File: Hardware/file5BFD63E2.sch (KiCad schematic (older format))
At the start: 14 parts, among them J18 Power_Connector_IO, J20 Digital_Connector_IO, J21 CV_Connector_IO, J22 Pot_Connector_IO, J23 Attenuverter_Connector_IO, J28 SID_Audio_Connector_IO

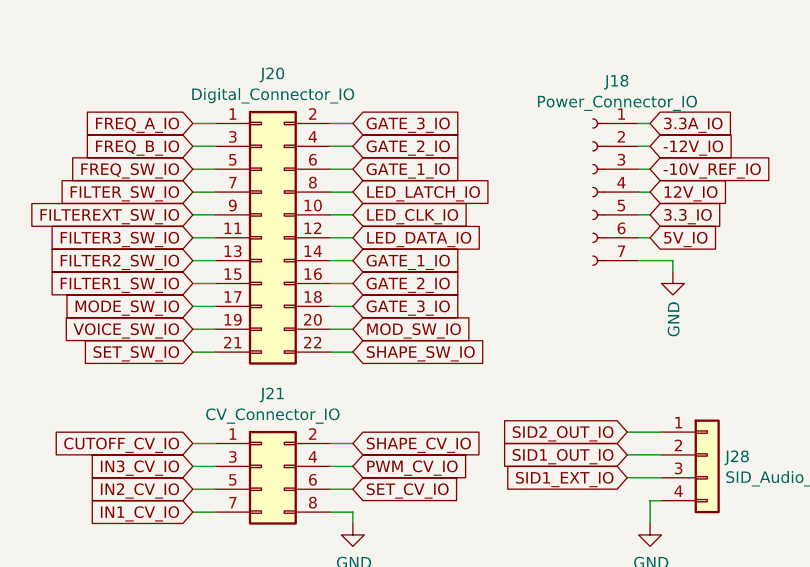
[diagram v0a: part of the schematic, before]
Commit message: Added some connector routing
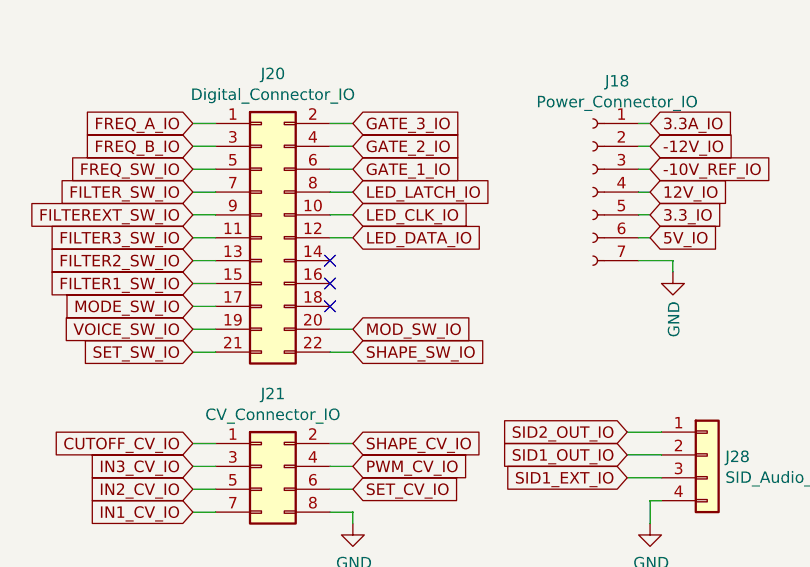
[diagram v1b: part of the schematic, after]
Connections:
- net GATE_1_IO: no longer J20.14 (Pin_14)
- net GATE_2_IO: no longer J20.16 (Pin_16)
- net GATE_3_IO: no longer J20.18 (Pin_18)
- no-connect marks 0 -> 3
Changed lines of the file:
@@
 Text GLabel 1750 3400 0    50   Input ~ 0
 FREQ_B_IO
-Text GLabel 2450 4100 2    50   Input ~ 0
-GATE_3_IO
-Text GLabel 2450 4000 2    50   Input ~ 0
-GATE_2_IO
-Text GLabel 2450 3900 2    50   Input ~ 0
-GATE_1_IO
 Text GLabel 2450 3800 2    50   Input ~ 0
 LED_DATA_IO
@@
 Wire Wire Line
 	2350 4200 2450 4200
-Wire Wire Line
-	2350 4100 2450 4100
-Wire Wire Line
-	2350 4000 2450 4000
-Wire Wire Line
-	2350 3900 2450 3900
 Wire Wire Line
 	2350 3800 2450 3800
@@
 	1    0    0    -1
 $EndComp
+NoConn ~ 2350 3900
+NoConn ~ 2350 4000
+NoConn ~ 2350 4100
 $EndSCHEMATC

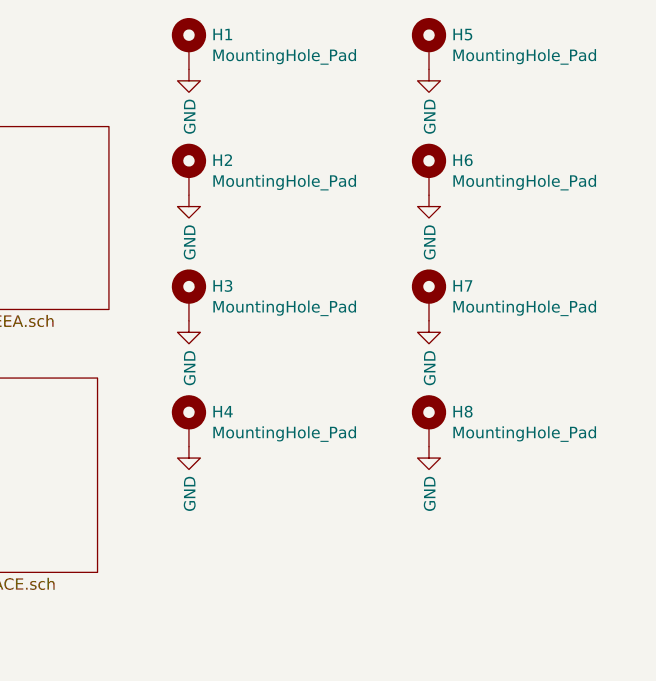
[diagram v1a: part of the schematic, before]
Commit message: Corrected layout and schematic to single standoff
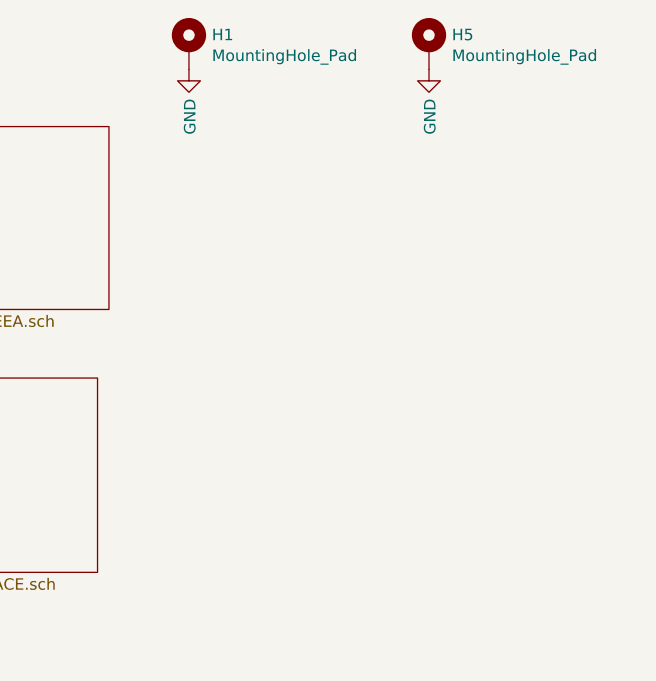
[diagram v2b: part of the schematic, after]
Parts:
- removed H2, H3, H4, H6, H7, H8: MountingHole_Pad, MountingHole:MountingHole_3.2mm_M3_DIN965_Pad, symbol Mechanical:MountingHole_Pad
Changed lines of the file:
@@
-$EndComp
-$Comp
-L Mechanical:MountingHole_Pad H6
-U 1 1 5BE3763A
-P 7100 2900
-F 0 "H6" H 7200 2951 50  0000 L CNN
-F 1 "MountingHole_Pad" H 7200 2860 50  0000 L CNN
-F 2 "MountingHole:MountingHole_3.2mm_M3_DIN965_Pad" H 7100 2900 50  0001 C CNN
-F 3 "~" H 7100 2900 50  0001 C CNN
-	1    7100 2900
-	1    0    0    -1
-$EndComp
-$Comp
-L Mechanical:MountingHole_Pad H7
-U 1 1 5BE3766D
-P 7100 3450
-F 0 "H7" H 7200 3501 50  0000 L CNN
-F 1 "MountingHole_Pad" H 7200 3410 50  0000 L CNN
-F 2 "MountingHole:MountingHole_3.2mm_M3_DIN965_Pad" H 7100 3450 50  0001 C CNN
-F 3 "~" H 7100 3450 50  0001 C CNN
-	1    7100 3450
-	1    0    0    -1
-$EndComp
-$Comp
-L Mechanical:MountingHole_Pad H8
-U 1 1 5BE376A0
-P 7100 4000
-F 0 "H8" H 7200 4051 50  0000 L CNN
-F 1 "MountingHole_Pad" H 7200 3960 50  0000 L CNN
-F 2 "MountingHole:MountingHole_3.2mm_M3_DIN965_Pad" H 7100 4000 50  0001 C CNN
-F 3 "~" H 7100 4000 50  0001 C CNN
-	1    7100 4000
-	1    0    0    -1
 $EndComp
 $Comp
@@
 	1    0    0    -1
 $EndComp
-$Comp
-L Mechanical:MountingHole_Pad H2
-U 1 1 5BE3F338
-P 6050 2900
-F 0 "H2" H 6150 2951 50  0000 L CNN
-F 1 "MountingHole_Pad" H 6150 2860 50  0000 L CNN
-F 2 "MountingHole:MountingHole_3.2mm_M3_DIN965_Pad" H 6050 2900 50  0001 C CNN
-F 3 "~" H 6050 2900 50  0001 C CNN
-	1    6050 2900
-	1    0    0    -1
-$EndComp
-$Comp
-L Mechanical:MountingHole_Pad H3
-U 1 1 5BE3F33F
-P 6050 3450
-F 0 "H3" H 6150 3501 50  0000 L CNN
-F 1 "MountingHole_Pad" H 6150 3410 50  0000 L CNN
-F 2 "MountingHole:MountingHole_3.2mm_M3_DIN965_Pad" H 6050 3450 50  0001 C CNN
-F 3 "~" H 6050 3450 50  0001 C CNN
-	1    6050 3450
-	1    0    0    -1
-$EndComp
-$Comp
-L Mechanical:MountingHole_Pad H4
-U 1 1 5BE3F346
-P 6050 4000
-F 0 "H4" H 6150 4051 50  0000 L CNN
-F 1 "MountingHole_Pad" H 6150 3960 50  0000 L CNN
-F 2 "MountingHole:MountingHole_3.2mm_M3_DIN965_Pad" H 6050 4000 50  0001 C CNN
-F 3 "~" H 6050 4000 50  0001 C CNN
-	1    6050 4000
-	1    0    0    -1
-$EndComp
-$Comp
-L power:GND #PWR?
-U 1 1 5BE41CB1
-P 6050 4100
-AR Path="/5C5B0291/5BE41CB1" Ref="#PWR?"  Part="1"
-AR Path="/5BFD63E3/5BE41CB1" Ref="#PWR0163"  Part="1"
-F 0 "#PWR0163" H 6050 3850 50  0001 C CNN
-F 1 "GND" V 6055 3972 50  0000 R CNN
-F 2 "" H 6050 4100 50  0001 C CNN
-F 3 "" H 6050 4100 50  0001 C CNN
-	1    6050 4100
-	1    0    0    -1
-$EndComp
-$Comp
-L power:GND #PWR?
-U 1 1 5BE41D02
-P 7100 4100
-AR Path="/5C5B0291/5BE41D02" Ref="#PWR?"  Part="1"
-AR Path="/5BFD63E3/5BE41D02" Ref="#PWR0164"  Part="1"
-F 0 "#PWR0164" H 7100 3850 50  0001 C CNN
-F 1 "GND" V 7105 3972 50  0000 R CNN
-F 2 "" H 7100 4100 50  0001 C CNN
-F 3 "" H 7100 4100 50  0001 C CNN
-	1    7100 4100
-	1    0    0    -1
-$EndComp
-$Comp
-L power:GND #PWR?
-U 1 1 5BE435B9
-P 6050 3000
-AR Path="/5C5B0291/5BE435B9" Ref="#PWR?"  Part="1"
-AR Path="/5BFD63E3/5BE435B9" Ref="#PWR0165"  Part="1"
-F 0 "#PWR0165" H 6050 2750 50  0001 C CNN
-F 1 "GND" V 6055 2872 50  0000 R CNN
-F 2 "" H 6050 3000 50  0001 C CNN
-F 3 "" H 6050 3000 50  0001 C CNN
-	1    6050 3000
-	1    0    0    -1
-$EndComp
-$Comp
-L power:GND #PWR?
-U 1 1 5BE435E0
-P 7100 3000
-AR Path="/5C5B0291/5BE435E0" Ref="#PWR?"  Part="1"
-AR Path="/5BFD63E3/5BE435E0" Ref="#PWR0166"  Part="1"
-F 0 "#PWR0166" H 7100 2750 50  0001 C CNN
-F 1 "GND" V 7105 2872 50  0000 R CNN
-F 2 "" H 7100 3000 50  0001 C CNN
-F 3 "" H 7100 3000 50  0001 C CNN
-	1    7100 3000
-	1    0    0    -1
-$EndComp
-$Comp
-L power:GND #PWR?
-U 1 1 5BE49823
-P 6050 3550
-AR Path="/5C5B0291/5BE49823" Ref="#PWR?"  Part="1"
-AR Path="/5BFD63E3/5BE49823" Ref="#PWR0167"  Part="1"
-F 0 "#PWR0167" H 6050 3300 50  0001 C CNN
-F 1 "GND" V 6055 3422 50  0000 R CNN
-F 2 "" H 6050 3550 50  0001 C CNN
-F 3 "" H 6050 3550 50  0001 C CNN
-	1    6050 3550
-	1    0    0    -1
-$EndComp
-$Comp
-L power:GND #PWR?
-U 1 1 5BE4984A
-P 7100 3550
-AR Path="/5C5B0291/5BE4984A" Ref="#PWR?"  Part="1"
-AR Path="/5BFD63E3/5BE4984A" Ref="#PWR0168"  Part="1"
-F 0 "#PWR0168" H 7100 3300 50  0001 C CNN
-F 1 "GND" V 7105 3422 50  0000 R CNN
-F 2 "" H 7100 3550 50  0001 C CNN
-F 3 "" H 7100 3550 50  0001 C CNN
-	1    7100 3550
-	1    0    0    -1
-$EndComp

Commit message: Swapped for real oscillator, fixed footprint discrepencies
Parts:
- J18: footprint Connector_PinSocket_2.54mm:PinSocket_1x07_P2.54mm_Vertical_SMD_Pin1Left -> Connector_PinSocket_2.54mm:PinSocket_1x07_P2.54mm_Vertical
- J21, J22: footprint Connector_PinSocket_2.54mm:PinSocket_2x04_P2.54mm_Vertical_SMD -> Connector_PinSocket_2.54mm:PinSocket_2x04_P2.54mm_Vertical
- J23, J28: footprint Connector_PinSocket_2.54mm:PinSocket_1x04_P2.54mm_Vertical_SMD_Pin1Left -> Connector_PinSocket_2.54mm:PinSocket_1x04_P2.54mm_Vertical
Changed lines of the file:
@@
 F 0 "J18" H 3394 4085 50  0000 C CNN
 F 1 "Power_Connector_IO" H 3394 3994 50  0000 C CNN
-F 2 "Connector_PinSocket_2.54mm:PinSocket_1x07_P2.54mm_Vertical_SMD_Pin1Left" H 3500 3600 50  0001 C CNN
+F 2 "Connector_PinSocket_2.54mm:PinSocket_1x07_P2.54mm_Vertical" H 3500 3600 50  0001 C CNN
 F 3 "~" H 3500 3600 50  0001 C CNN
 	1    3500 3600
@@
 F 0 "J21" H 2100 5117 50  0000 C CNN
 F 1 "CV_Connector_IO" H 2100 5026 50  0000 C CNN
-F 2 "Connector_PinSocket_2.54mm:PinSocket_2x04_P2.54mm_Vertical_SMD" H 2050 4800 50  0001 C CNN
+F 2 "Connector_PinSocket_2.54mm:PinSocket_2x04_P2.54mm_Vertical" H 2050 4800 50  0001 C CNN
 F 3 "~" H 2050 4800 50  0001 C CNN
 	1    2050 4800
@@
 F 0 "J22" H 2100 5967 50  0000 C CNN
 F 1 "Pot_Connector_IO" H 2100 5876 50  0000 C CNN
-F 2 "Connector_PinSocket_2.54mm:PinSocket_2x04_P2.54mm_Vertical_SMD" H 2050 5650 50  0001 C CNN
+F 2 "Connector_PinSocket_2.54mm:PinSocket_2x04_P2.54mm_Vertical" H 2050 5650 50  0001 C CNN
 F 3 "~" H 2050 5650 50  0001 C CNN
 	1    2050 5650
@@
 F 0 "J23" H 2129 6192 50  0000 L CNN
 F 1 "Attenuverter_Connector_IO" H 2129 6101 50  0000 L CNN
-F 2 "Connector_PinSocket_2.54mm:PinSocket_1x04_P2.54mm_Vertical_SMD_Pin1Left" H 2050 6200 50  0001 C CNN
+F 2 "Connector_PinSocket_2.54mm:PinSocket_1x04_P2.54mm_Vertical" H 2050 6200 50  0001 C CNN
 F 3 "~" H 2050 6200 50  0001 C CNN
 	1    2050 6200
@@
 F 0 "J28" H 4079 4742 50  0000 L CNN
 F 1 "SID_Audio_Connector_IO" H 4079 4651 50  0000 L CNN
-F 2 "Connector_PinSocket_2.54mm:PinSocket_1x04_P2.54mm_Vertical_SMD_Pin1Left" H 4000 4750 50  0001 C CNN
+F 2 "Connector_PinSocket_2.54mm:PinSocket_1x04_P2.54mm_Vertical" H 4000 4750 50  0001 C CNN
 F 3 "~" H 4000 4750 50  0001 C CNN
 	1    4000 4750

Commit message: Fixes #10
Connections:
- net LED_BLANK_IO: now reaches J20.18 (Pin_18)
- no-connect marks 3 -> 2
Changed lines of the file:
@@
 NoConn ~ 2350 3900
 NoConn ~ 2350 4000
-NoConn ~ 2350 4100
+Text GLabel 2450 4100 2    50   Input ~ 0
+LED_BLANK_IO
+Wire Wire Line
+	2450 4100 2350 4100
 $EndSCHEMATC
